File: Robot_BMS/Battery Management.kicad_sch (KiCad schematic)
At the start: 27 parts, among them IC2 BQ76922RSNR, Q2 SIS413DN-T1-GE3, Q3 2N7002, Q4 SIS413DN-T1-GE3

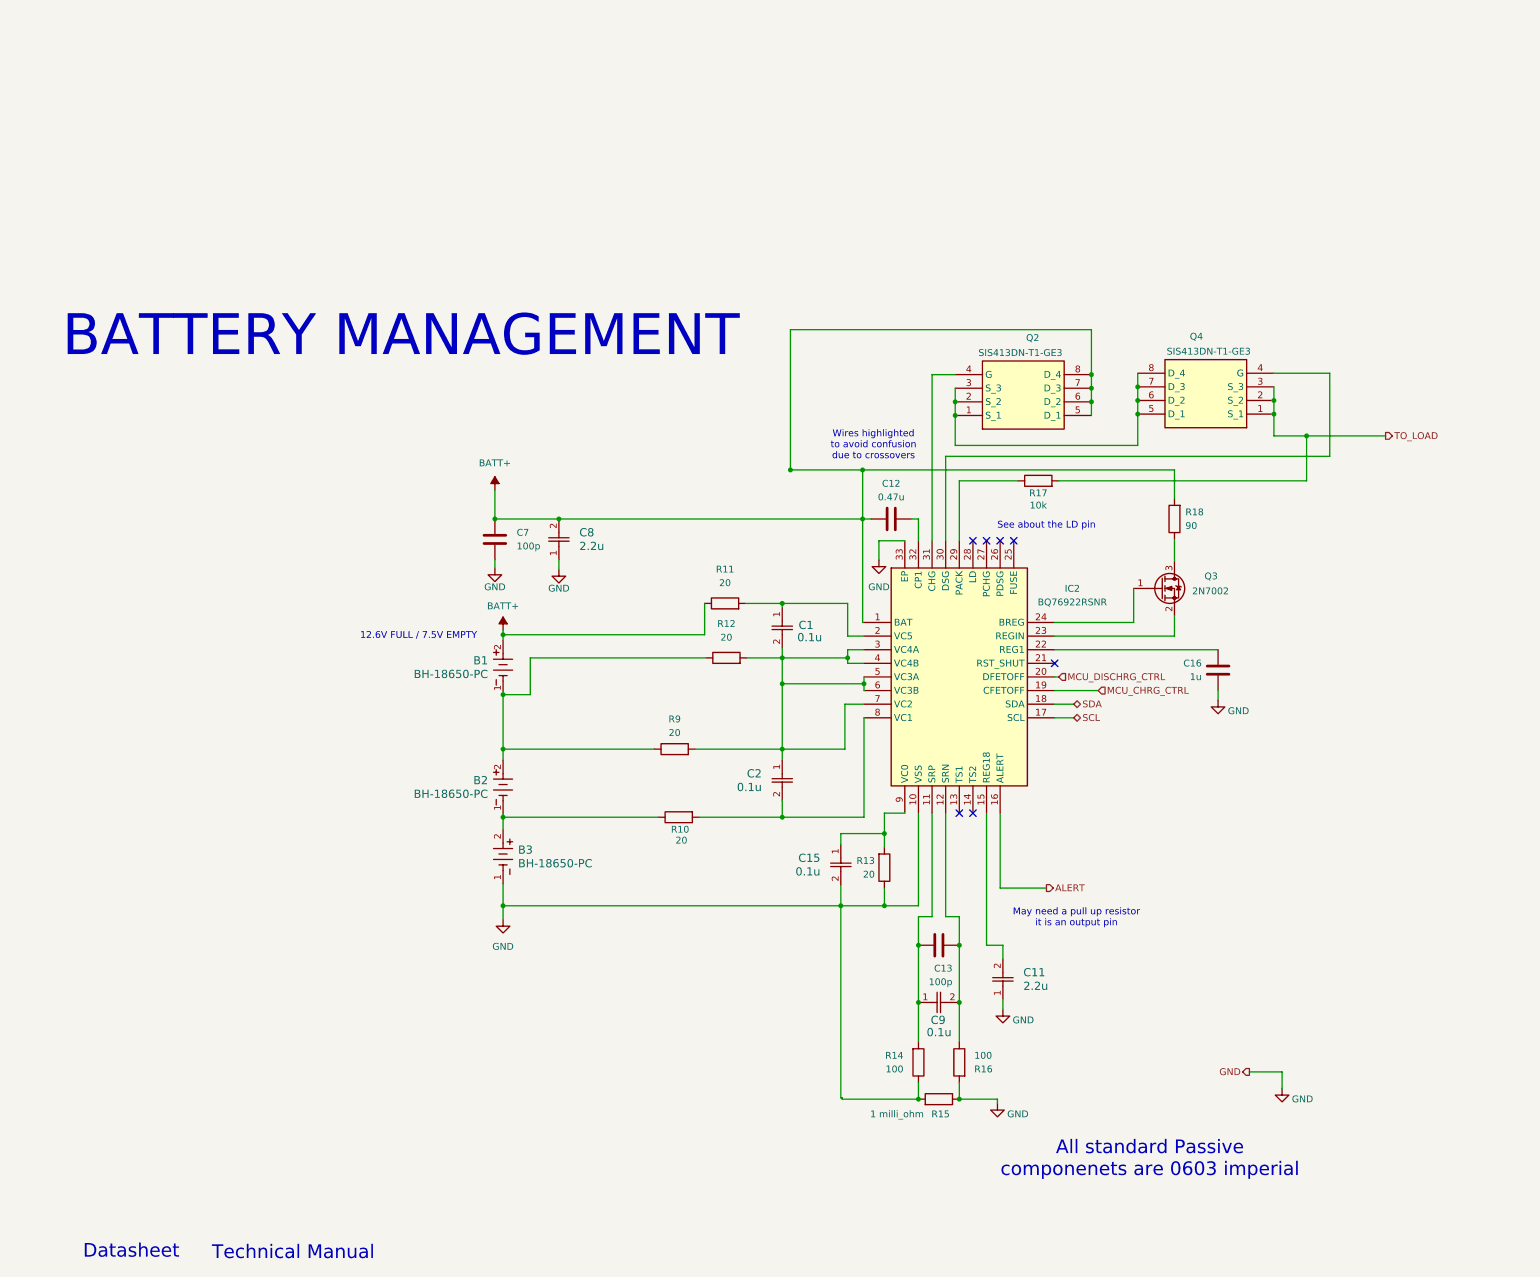
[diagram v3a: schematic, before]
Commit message: still adding in symbols & footprints for passives
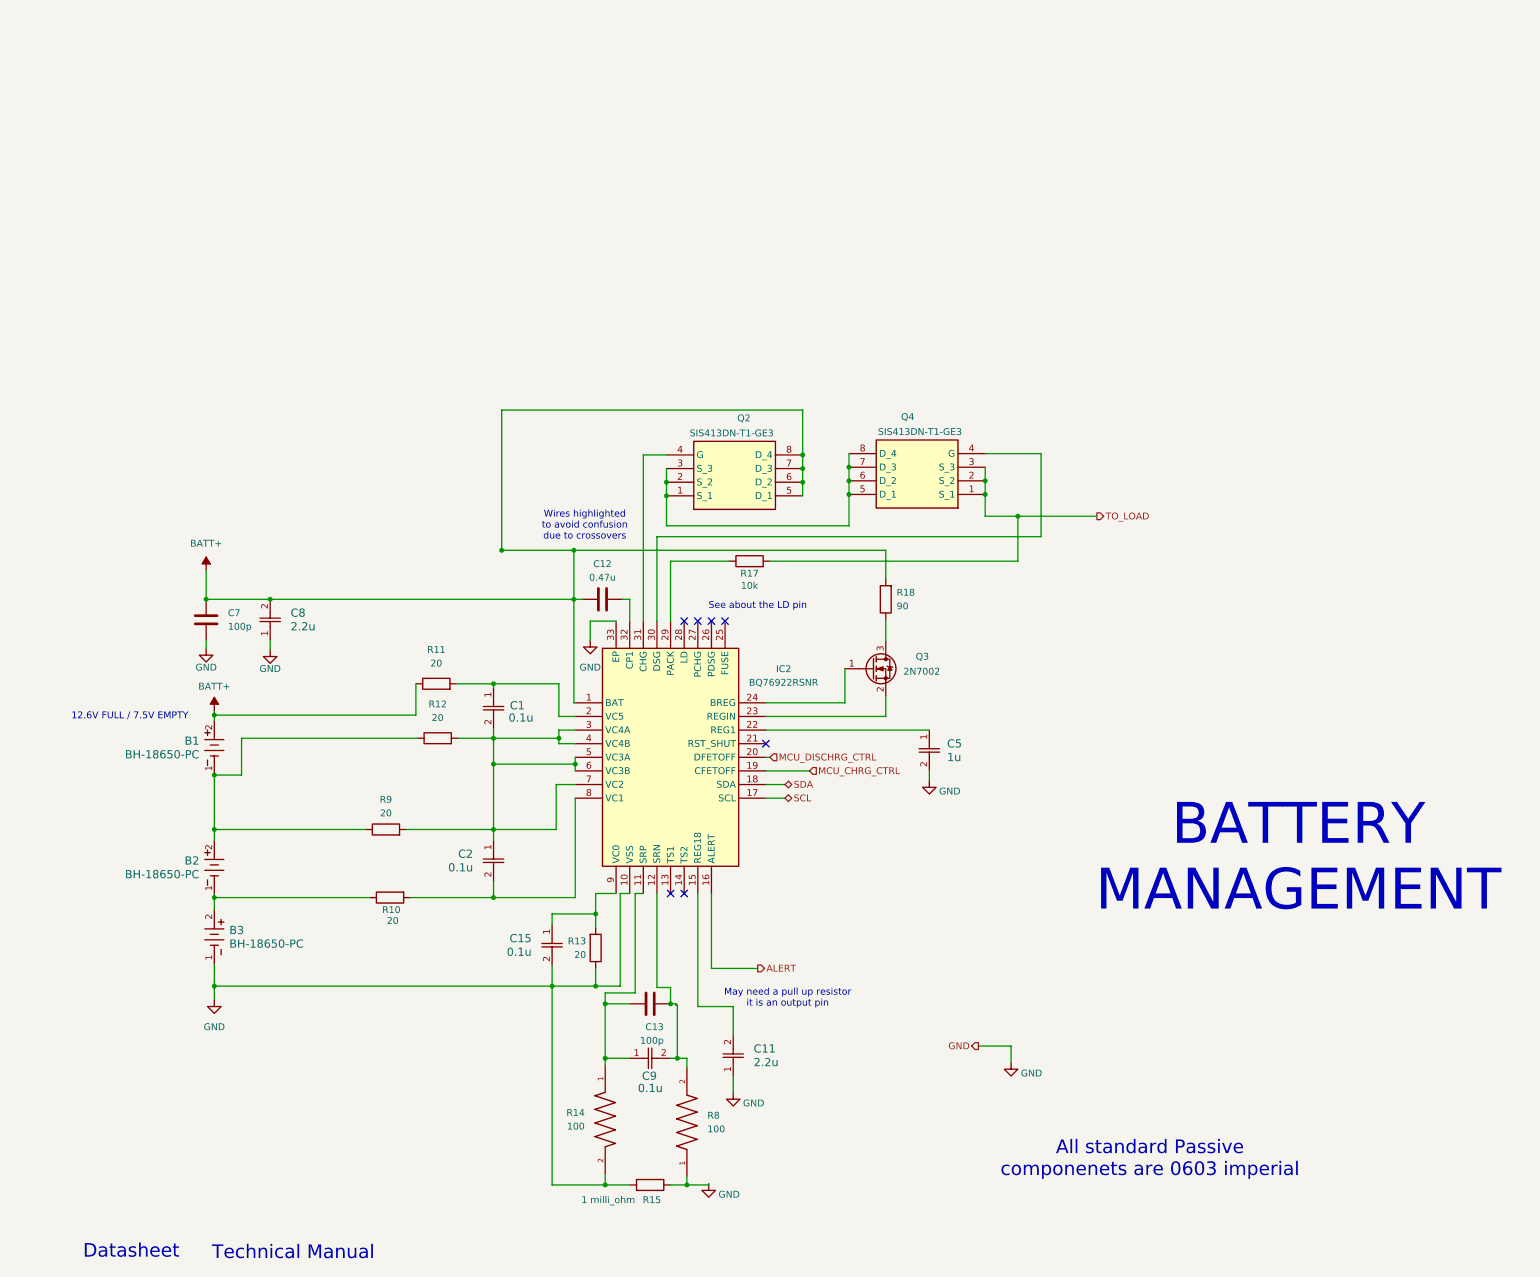
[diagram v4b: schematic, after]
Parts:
- removed C16: 1u, symbol Device:C
- removed R14, R16: 100, symbol Device:R
- added C5: 1u, CAP_1608_TDK, symbol C1608X5R1H105K080AB:C1608X5R1H105K080AB
- added R14, R8: 100, AT0603DRE07100RL:RESC1608X55N, symbol AT0603DRE07100RL:AT0603DRE07100RL
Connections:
- net GND: now also C5.2, R14.2, R8.1
- net at C13.2, C9.1, IC2.11 (SRP): now also R14.1
- net at C13.1, C9.2, IC2.12 (SRN): now also R8.2
- net at IC2.22 (REG1): now also C5.1
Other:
- moved on the sheet: B1, B2, B3, C1, C11, C12, C13, C15, C2, C7, C8, C9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

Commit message: all symbols footprints & models added
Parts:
- removed C12: 0.47u, symbol Device:C
- removed C13, C7: 100p, symbol Device:C
- removed R10, R11, R12, R13, R9: 20, symbol Device:R
- removed R15: 1 milli_ohm, symbol Device:R
- removed R17: 10k, symbol Device:R
- removed R18: 90, symbol Device:R
- added C12: 0.47u, RobotBMS:CAP_1608_TDK, symbol C1608X5R1H474K080AB:C1608X5R1H474K080AB
- added C14, C7: 100p, RobotBMS:CAPC1608X97N, symbol GA0603A101JXBAC31G:GA0603A101JXBAC31G
- added R10, R11, R12, R13, R9: 20, RobotBMS:RES_ERJPA3F20R0V, symbol ERJPA3F20R0V:ERJPA3F20R0V
- added R15: 1 mOhm, RobotBMS:RC0603N_YAG, symbol 580060716002:RC0603FR-073K24L
- added R17: 10k, RobotBMS:RC0603N_YAG, symbol RC0603FR-0710KL:RC0603FR-0710KL
- added R18: 100, RobotBMS:RESC1608X55N, symbol AT0603DRE07100RL:AT0603DRE07100RL
- C10: renamed from C1; footprint CAPC17595_87N_KEM -> RobotBMS:CAPC17595_87N_KEM
- C11: renamed from C2; footprint CAPC17595_87N_KEM -> RobotBMS:CAPC17595_87N_KEM
- C13: renamed from C9; footprint CAPC17595_87N_KEM -> RobotBMS:CAPC17595_87N_KEM
- C16: renamed from C5; footprint CAP_1608_TDK -> RobotBMS:CAP_1608_TDK
- C9: renamed from C15; footprint CAPC17595_87N_KEM -> RobotBMS:CAPC17595_87N_KEM
- R14: footprint AT0603DRE07100RL:RESC1608X55N -> RobotBMS:RESC1608X55N
- R16: renamed from R8; footprint AT0603DRE07100RL:RESC1608X55N -> RobotBMS:RESC1608X55N
- renumbered C11 to C15
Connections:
- net BATT+: now also C12.1, C7.1, R12.1, R18.2
- net GND: now also C7.2, R13.1, R15.1, R15.2
- net TO_LOAD: now also R17.2
- net at C13.1, IC2.11 (SRP), R14.1: now also C14.1
- net at C13.2, IC2.12 (SRN), R16.2: now also C14.2
- net at C10.1, IC2.2 (VC5): now also R12.2
- net at IC2.29 (PACK): now also R17.1
- net at C10.2, C11.1, IC2.3 (VC4A)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: now also R10.2, R11.2
- net at IC2.32 (CP1): now also C12.2
- net at C11.2, IC2.8 (VC1): now also R9.2
- net at C9.1, IC2.9 (VC0): now also R13.2
- net at B1.1, B2.2: now also R10.1, R11.1
- net at B2.1, B3.2: now also R9.1
- net at Q3.3 (D): now also R18.1
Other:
- moved on the sheet: C9, Q3

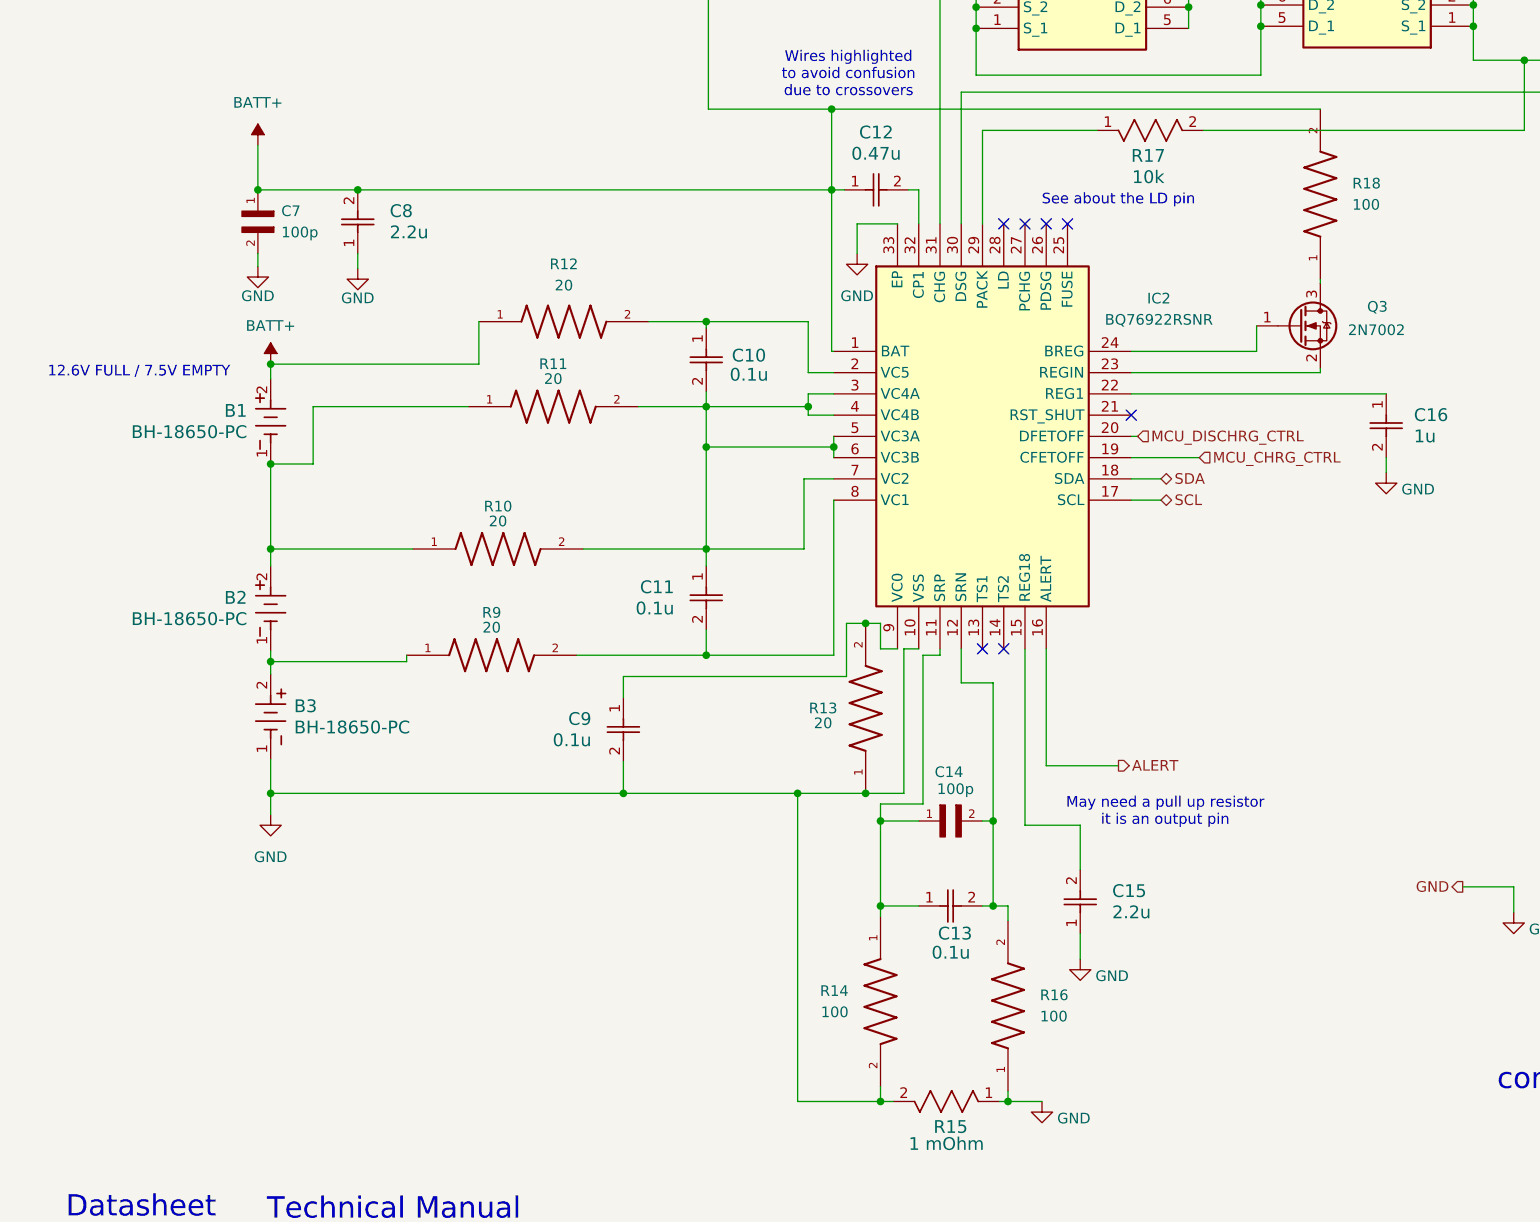
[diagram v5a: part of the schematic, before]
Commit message: BOM done, with total price £40
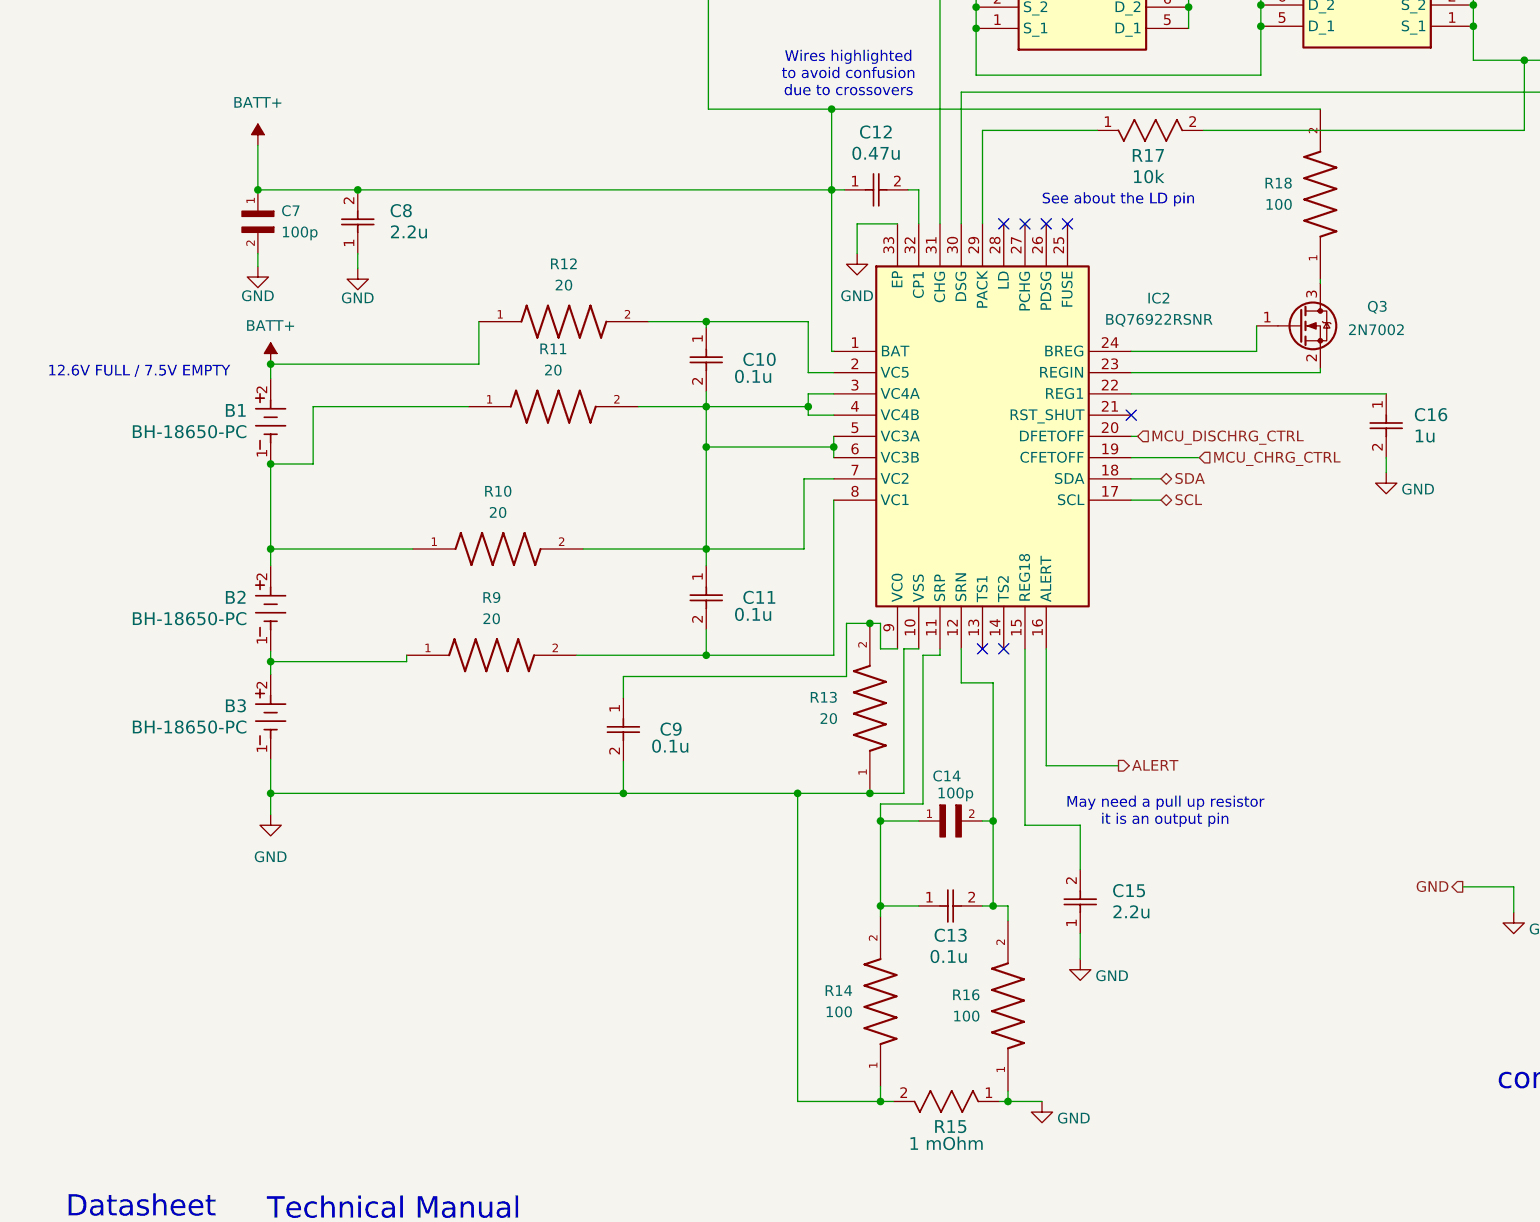
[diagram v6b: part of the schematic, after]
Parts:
- B1, B2, B3: Manufacturer_Part_Number (none) -> BH-18650-PC; Price (none) -> 3.08
- C10, C11, C13, C9: Manufacturer_Part_Number (none) -> C0603C104K5RACAUTO; Price (none) -> 0.05
- C12: Manufacturer_Part_Number (none) -> C1608X5R1H474K080AB; Price (none) -> 0.156
- C14, C7: Manufacturer_Part_Number (none) -> GA0603A101JXBAC31G; Price None -> 0.204
- C15, C8: Manufacturer_Part_Number (none) -> GRM188R61H225KE11D; Price (none) -> 0.22
- C16: Manufacturer_Part_Number (none) -> C1608X5R1H105K080AB; Price (none) -> 0.156
- IC2: Price (none) -> 3.08
- Q2, Q4: Price (none) -> 0.58
- Q3: Manufacturer_Part_Number (none) -> 2N7002 H6327; Price (none) -> 0.21
- R10, R11, R12, R13, R9: Manufacturer_Part_Number (none) -> ERJPA3F20R0V; Price None -> 0.0512
- R14, R16, R18: Manufacturer_Part_Number (none) -> AT0603DRE07100RL; Price None -> 0.068
- R15: Manufacturer_Part_Number (none) -> 580060716002; Price (none) -> 0.445
- R17: Manufacturer_Part_Number (none) -> RC0603FR-0710KL; Price (none) -> 0.096
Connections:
- net GND: now also R14.1; no longer R14.2
- net at C13.1, C14.1, IC2.11 (SRP): now also R14.2; no longer R14.1
